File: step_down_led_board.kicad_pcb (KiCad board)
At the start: 2 copper layers, 29.2 x 50.8 mm, 34 parts, among them CON1 BARREL_JACK, J1 OSHW Logo, J2 Polarity Mark, M1 BuckModule, M2 BuckModule, P1 CONN_02X20, P2 CONN_01X02, P3 CONN_01X05, P4 CONN_01X02, P5 CONN_01X02, P6 CONN_01X03, P9 CONN_01X06, Q1 Q_NMOS_GSD, Q2 Q_NMOS_GSD, Q3 Q_NMOS_GSD, Q4 Q_NMOS_GSD, Q5 Q_NMOS_GSD, Q9 Q_NMOS_GSD

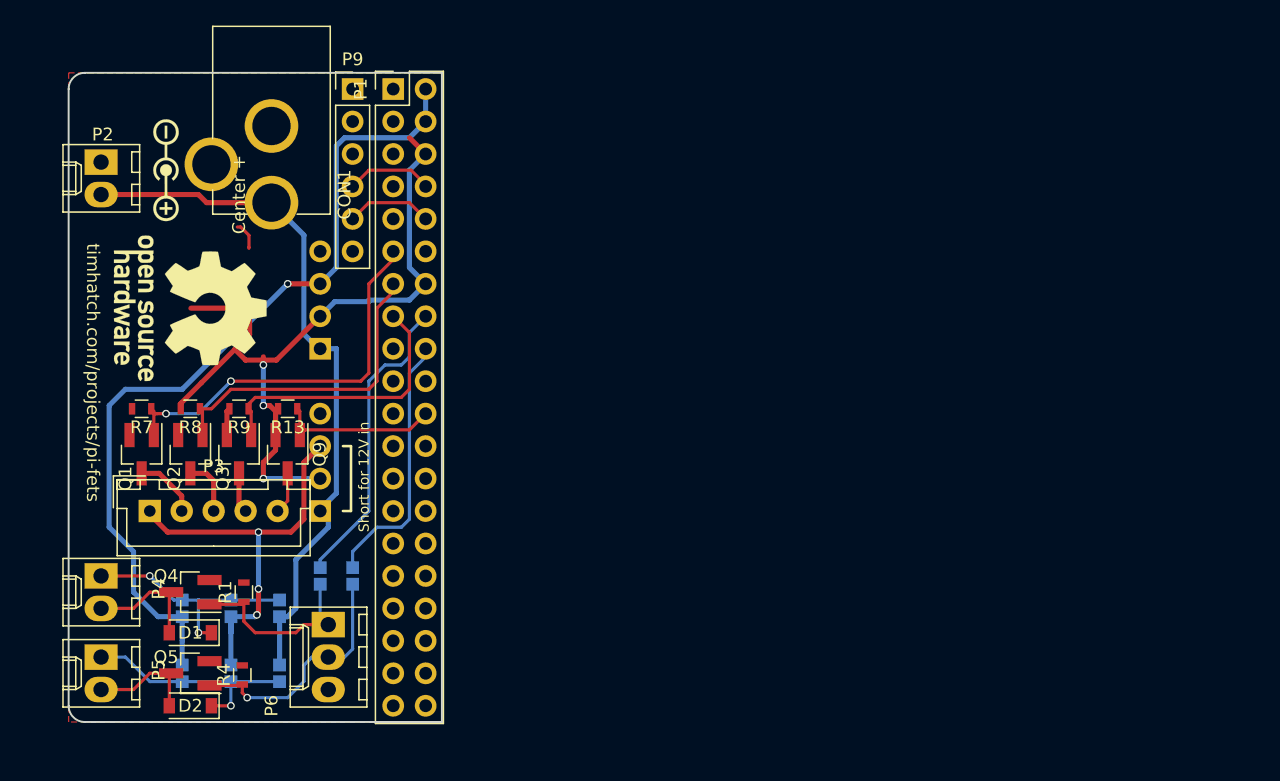
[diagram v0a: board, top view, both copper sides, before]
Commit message: Include buck converter on board.
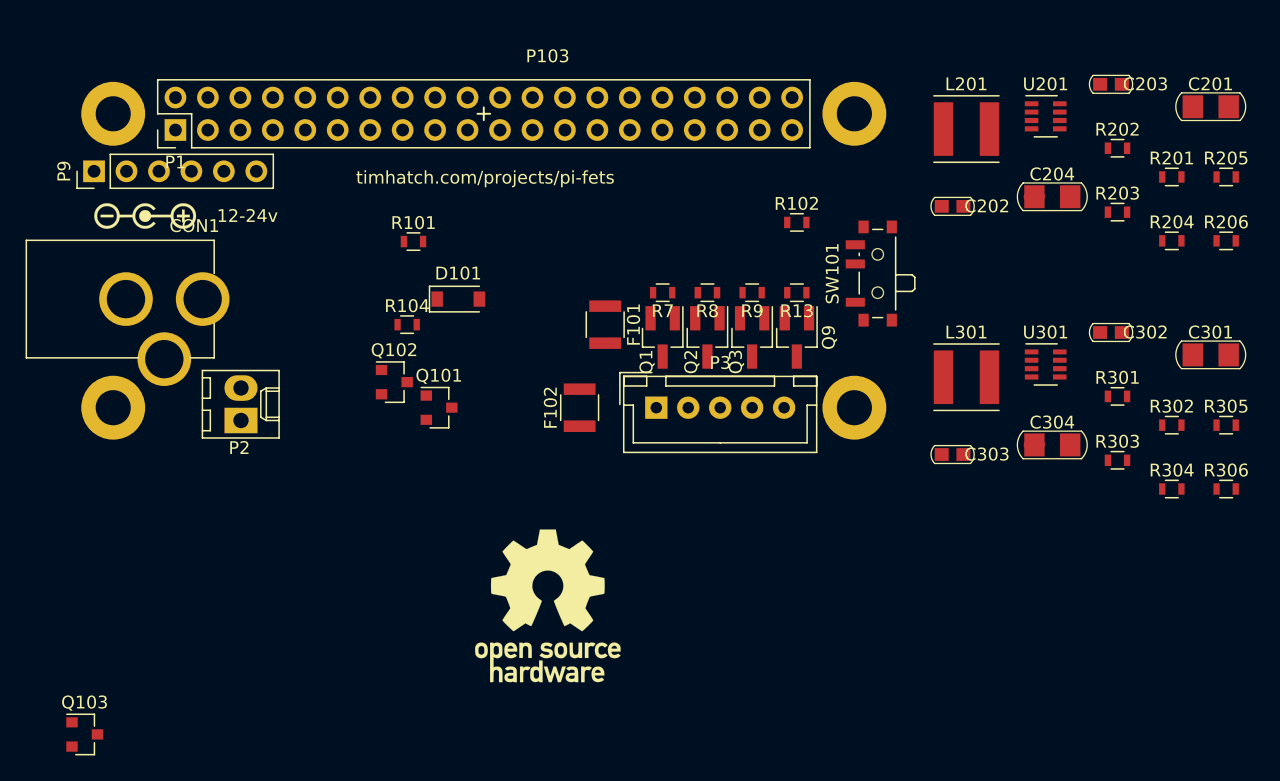
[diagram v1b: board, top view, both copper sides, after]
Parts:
- removed D1, D2: D, Diodes_SMD:D_SOD-123
- removed J1: OSHW Logo, Symbols:OSHW-Logo_11.4x12mm_SilkScreen
- removed J2: Polarity Mark, Polarity:Polarity_Center_Positive_2mm_SilkScreen
- removed JP1, JP2, JP3, JP4, JP5, JP6, JP7, JP8: Jumper_NO_Small, jumper:SOLDER-JUMPER_1-WAY
- removed M1, M2: BuckModule, BuckModule-Tim:BuckModule
- removed P4, P5: CONN_01X02, Connectors_Molex:Molex_KK-6410-02_02x2.54mm_Straight
- removed P6: CONN_01X03, Connectors_Molex:Molex_KK-6410-03_03x2.54mm_Straight
- removed Q4, Q5: Q_NMOS_GSD, TO_SOT_Packages_SMD:SOT-23_Handsoldering
- removed R1, R4: 10K, Resistors_SMD:R_0603
- added C201: 22u, Capacitors_SMD_Round:C_1206, F.Cu at (232.9, 76.9)
- added C202: 0.1u, Capacitors_SMD_Round:C_0603, F.Cu at (212.7, 84.7)
- added C203: 0.1u, Capacitors_SMD_Round:C_0603, F.Cu at (225.1, 75.2)
- added C204: 44u, Capacitors_SMD_Round:C_1206_NetTie, F.Cu at (220.5, 84.0)
- added C301: 22u, Capacitors_SMD_Round:C_1206, F.Cu at (232.9, 96.4)
- added C302: 0.1u, Capacitors_SMD_Round:C_0603, F.Cu at (225.1, 94.6)
- added C303: 0.1u, Capacitors_SMD_Round:C_0603, F.Cu at (212.7, 104.2)
- added C304: 44u, Capacitors_SMD_Round:C_1206_NetTie, F.Cu at (220.5, 103.4)
- added D101: 10V, Diodes_SMD:D_SOD-123, F.Cu at (174.0, 92.0)
- added F101: Polyfuse, Resistors_SMD:R_1210, F.Cu at (185.5, 94.0)
- added F102: Polyfuse, Resistors_SMD:R_1210, F.Cu at (183.5, 100.5)
- added L201: L, Inductors_SMD:L_Taiyo-Yuden_MD-5050, F.Cu at (213.8, 78.7)
- added L301: L, Inductors_SMD:L_Taiyo-Yuden_MD-5050, F.Cu at (213.8, 98.1)
- added P101: Polarity, Polarity_Symbols:Polarity_Center_Positive_2mm_SilkScreen, F.Cu at (149.5, 85.5)
- added P102: OSHW, Symbols:OSHW-Logo_11.4x12mm_SilkScreen, F.Cu at (181.0, 116.0)
- added P103: SYMBOL, Board_Outlines:Pi_Zero, F.Cu at (176.0, 77.5)
- added Q101: AO3401A, TO_SOT_Packages_SMD:SOT-23, F.Cu at (172.5, 100.5)
- added Q102: AO3401A, TO_SOT_Packages_SMD:SOT-23, F.Cu at (169.0, 98.5)
- added Q103: AO3401A, TO_SOT_Packages_SMD:SOT-23, F.Cu at (144.8, 126.1)
- added R101: 100k, Resistors_SMD:R_0603, F.Cu at (170.5, 87.5)
- added R102: 1k, Resistors_SMD:R_0603, F.Cu at (200.5, 86.0)
- added R104: 100k, Resistors_SMD:R_0603, F.Cu at (170.0, 94.0)
- added R201: 100k, Resistors_SMD:R_0603, F.Cu at (229.8, 82.4)
- added R202: 75k, Resistors_SMD:R_0603, F.Cu at (225.6, 80.2)
- added R203: 20R, Resistors_SMD:R_0603, F.Cu at (225.6, 85.2)
- added R204: R, Resistors_SMD:R_0603, F.Cu at (229.8, 87.4)
- added R205: R, Resistors_SMD:R_0603, F.Cu at (234.1, 82.4)
- added R206: R, Resistors_SMD:R_0603, F.Cu at (234.1, 87.4)
- added R301: 100k, Resistors_SMD:R_0603, F.Cu at (225.6, 99.6)
- added R302: 75k, Resistors_SMD:R_0603, F.Cu at (229.8, 101.9)
- added R303: 20R, Resistors_SMD:R_0603, F.Cu at (225.6, 104.6)
- added R304: R, Resistors_SMD:R_0603, F.Cu at (229.8, 106.9)
- added R305: R, Resistors_SMD:R_0603, F.Cu at (234.1, 101.9)
- added R306: R, Resistors_SMD:R_0603, F.Cu at (234.1, 106.9)
- added SW101: SW_SPDT, Buttons_Switches_SMD:SW_SPDT_PCM12, F.Cu at (206.5, 90.0)
- added U201: MP2315, TO_SOT_Packages_SMD:SOT-23-8, F.Cu at (220.0, 77.7)
- added U301: MP2315, TO_SOT_Packages_SMD:SOT-23-8, F.Cu at (220.0, 97.1)
- moved Q1 41.8 mm to (190.0, 95.0)
- moved R7 41.8 mm to (190.0, 91.5)
- moved Q2 41.5 mm to (193.5, 95.0)
- moved R8 41.5 mm to (193.5, 91.5)
- moved Q3 41.2 mm to (197.0, 95.0)
- moved R9 41.2 mm to (197.0, 91.5)
- moved Q9 40.9 mm to (200.5, 95.0)
- moved R13 40.9 mm to (200.5, 91.5)
- moved P3 40.5 mm to (189.5, 100.5)
- moved P2 23.0 mm to (157.0, 101.5), turned to 90 degrees
- moved P9 21.2 mm to (145.5, 82.0), turned to 90 degrees
- moved P1 17.3 mm to (151.9, 78.8), turned to 90 degrees
- moved CON1 9.27 mm to (154.0, 92.0), turned to 0 degrees
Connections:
- P1 pad 16: Net-(JP7-Pad2) -> (no net)
- P1 pad 18: Net-(JP8-Pad2) -> (no net)
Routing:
- net +5V: track 66.7 -> 0.00 mm, vias 1 -> 0
- net GND: track 63.2 -> 0.00 mm, vias 3 -> 0
- net +24V: track 57.7 -> 0.00 mm
- net +12V: track 34.5 -> 0.00 mm, vias 3 -> 0
- net R_PIN: track 31.6 -> 0.00 mm, vias 2 -> 0
- net G_PIN: track 25.8 -> 0.00 mm
- net Net-(JP7-Pad2): track 23.8 -> 0.00 mm
- net B_PIN: track 21.8 -> 0.00 mm
- net Net-(JP8-Pad2): track 20.6 -> 0.00 mm
- net EXT_B: track 19.4 -> 0.00 mm, vias 1 -> 0
- net Net-(D1-Pad1): track 18.4 -> 0.00 mm, vias 2 -> 0
- net Net-(D2-Pad1): track 18.2 -> 0.00 mm, vias 1 -> 0
- net EXT_A: track 15.0 -> 0.00 mm
- net W_PIN: track 12.7 -> 0.00 mm
- net Net-(D1-Pad2): track 9.25 -> 0.00 mm
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- removed copper zone on F.Cu, net GND
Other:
- board outline removed
- board text added: "12-24v"
- board text removed: "12"
- board text removed: "12V"
- board text removed: "24"
- board text removed: "5V"
- board text removed: "Buck modules this side"
- board text removed: "Center +"
- board text removed: "Short for 12V in"

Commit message: Massive changes, including makefile
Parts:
- removed F101, F102: Polyfuse, Resistors_SMD:R_1210
- added D2: LED, LEDs:LED_0805, F.Cu at (165.2, 83.0)
- added D3: LED, LEDs:LED_0805, F.Cu at (182.8, 92.2)
- added F1: Polyfuse, Resistors_SMD:R_1812, F.Cu at (162.0, 84.0)
- added F2: Polyfuse, Resistors_SMD:R_1812, F.Cu at (185.8, 94.2)
- added P6: US0001, OSHWA_Certification_Mark:OSHW_Mono_0.25_Scale, F.Cu at (172.8, 90.2)
- added R4: 1k, Resistors_SMD:R_0603, F.Cu at (165.2, 86.8)
- added R5: 2k, Resistors_SMD:R_0603, F.Cu at (182.8, 95.8)
- C201, C204, C301, C304, L201, L301, R201, R202, R203, R204, R205, R206, R301, R302, R303, R304, R305, R306, U201, U301: moved to B.Cu
- C202, C203, C302, C303: footprint Capacitors_SMD_Round:C_0603 -> Capacitors_SMD:C_0603; moved to B.Cu
- P5: renamed from P102; moved to B.Cu
- moved C201 73.9 mm to (161.0, 94.0), turned to 90 degrees
- moved R206 69.7 mm to (165.0, 96.2), turned to 90 degrees
- moved R205 67.5 mm to (168.0, 96.2), turned to 270 degrees
- moved R202 64.1 mm to (163.5, 96.2), turned to 270 degrees
- moved R204 64.0 mm to (166.5, 96.2), turned to 90 degrees
- moved R201 61.9 mm to (169.5, 96.2), turned to 90 degrees
- moved C204 59.6 mm to (161.0, 88.2), turned to 270 degrees
- moved C301 57.9 mm to (175.0, 94.0), turned to 90 degrees
- moved U201 57.2 mm to (164.9, 93.1)
- moved C203 57.0 mm to (169.4, 87.1), turned to 90 degrees
- moved R203 56.5 mm to (169.4, 90.4), turned to 270 degrees
- moved R306 56.1 mm to (179.0, 96.2), turned to 90 degrees
- moved R302 52.6 mm to (177.5, 96.2), turned to 270 degrees
- moved R305 52.4 mm to (182.0, 96.2), turned to 270 degrees
- moved R304 50.5 mm to (180.5, 96.2), turned to 90 degrees
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- renumbered D101 to D1, CON1 to P1, P103 to P3, P101 to P4, P1 to P7, P9 to P8, P3 to P9, Q101 to Q1, Q103 to Q2, Q102 to Q3, Q1 to Q4, Q2 to Q5, Q3 to Q6, Q9 to Q7, R101 to R1, R102 to R2, R104 to R3, R7 to R6, R8 to R7, R9 to R8, R13 to R9, SW101 to SW1
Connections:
- Q1 pad 3: Net-(F102-Pad2) -> Net-(F2-Pad2)
- Q2 pad 2: Net-(F102-Pad2) -> Net-(Q2-Pad2)
- Q2 pad 3: Net-(Q102-Pad3) -> /buck2/VOUT
- Q3 pad 2: /buck2/VOUT -> Net-(Q2-Pad2)
- Q3 pad 3: Net-(Q102-Pad3) -> Net-(F2-Pad2)
- R3 pad 1: /buck2/VOUT -> Net-(Q2-Pad2)
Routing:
- net +24V: track 0.00 -> 70.5 mm, vias 0 -> 12
- net Net-(Q2-Pad1): track 0.00 -> 51.4 mm, vias 0 -> 2
- net Net-(D1-Pad2): track 0.00 -> 47.6 mm, vias 0 -> 4
- net GND: track 0.00 -> 43.2 mm, vias 0 -> 7
- net R_PIN: track 0.00 -> 39.6 mm
- net B_PIN: track 0.00 -> 38.5 mm
- net G_PIN: track 0.00 -> 38.4 mm
- net W_PIN: track 0.00 -> 38.3 mm
- net Net-(F2-Pad2): track 0.00 -> 22.1 mm
- net +5V: track 0.00 -> 19.3 mm, vias 0 -> 1
- net /buck2/VOUT: track 0.00 -> 18.1 mm, vias 0 -> 1
- net +12V: track 0.00 -> 14.0 mm, vias 0 -> 1
- net Net-(C204-Pad1): track 0.00 -> 13.8 mm, vias 0 -> 2
- net Net-(C304-Pad1): track 0.00 -> 13.3 mm, vias 0 -> 2
- net TXD: track 0.00 -> 11.0 mm
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- added copper zone on B.Cu, net +24V
- added copper zone on F.Cu, net +24V
- added copper zone on B.Cu, net GND
- added copper zone on B.Cu, net Net-(C203-Pad2)
- added copper zone on B.Cu, net Net-(C204-Pad1)
- added copper zone on B.Cu, net Net-(C303-Pad2)
- added copper zone on B.Cu, net Net-(C304-Pad1)
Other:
- board outline added: 65 x 30 mm
- board text added: "+"
- board text added: "-"
- board text added: "12v"
- board text added: "24v"
- board text added: "CC-BY"
- board text added: "Pins: 11, 13, 15, 22"
- board text added: "branch:v1.x"

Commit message: Update OSH Certification
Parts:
- P6: value US0001 -> US0118
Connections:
- P7 pad 1: (no net) -> Net-(P7-Pad1)
- P7 pad 12: (no net) -> Net-(P7-Pad12)
- P7 pad 16: (no net) -> Net-(P7-Pad16)
- P7 pad 17: (no net) -> Net-(P7-Pad17)
- P7 pad 18: (no net) -> Net-(P7-Pad18)
- P7 pad 19: (no net) -> Net-(P7-Pad19)
- P7 pad 20: (no net) -> Net-(P7-Pad20)
- P7 pad 21: (no net) -> Net-(P7-Pad21)
- P7 pad 23: (no net) -> Net-(P7-Pad23)
- P7 pad 24: (no net) -> Net-(P7-Pad24)
- P7 pad 25: (no net) -> Net-(P7-Pad25)
- P7 pad 26: (no net) -> Net-(P7-Pad26)
- P7 pad 27: (no net) -> Net-(P7-Pad27)
- P7 pad 28: (no net) -> Net-(P7-Pad28)
- P7 pad 29: (no net) -> Net-(P7-Pad29)
- P7 pad 3: (no net) -> Net-(P7-Pad3)
- P7 pad 30: (no net) -> Net-(P7-Pad30)
- P7 pad 31: (no net) -> Net-(P7-Pad31)
- P7 pad 32: (no net) -> Net-(P7-Pad32)
- P7 pad 33: (no net) -> Net-(P7-Pad33)
- P7 pad 34: (no net) -> Net-(P7-Pad34)
- P7 pad 35: (no net) -> Net-(P7-Pad35)
- P7 pad 36: (no net) -> Net-(P7-Pad36)
- P7 pad 37: (no net) -> Net-(P7-Pad37)
- P7 pad 38: (no net) -> Net-(P7-Pad38)
- P7 pad 39: (no net) -> Net-(P7-Pad39)
- P7 pad 40: (no net) -> Net-(P7-Pad40)
- P7 pad 5: (no net) -> Net-(P7-Pad5)
- P7 pad 7: (no net) -> Net-(P7-Pad7)
- P7 pad 9: (no net) -> Net-(P7-Pad9)
- P8 pad 2: (no net) -> Net-(P8-Pad2)
- P8 pad 3: (no net) -> Net-(P8-Pad3)
- P8 pad 6: (no net) -> Net-(P8-Pad6)
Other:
- board text added: "v1.0"
